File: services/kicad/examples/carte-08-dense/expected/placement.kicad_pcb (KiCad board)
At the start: 2 copper layers, 57.3 x 44 mm, 56 parts, among them J1 IN_5V, J10 IO0, J11 IO1, J12 IO2, J13 IO3, J14 IO4, J2 SWD, U1 STM32F103C8T6, U2 AMS1117-3.3

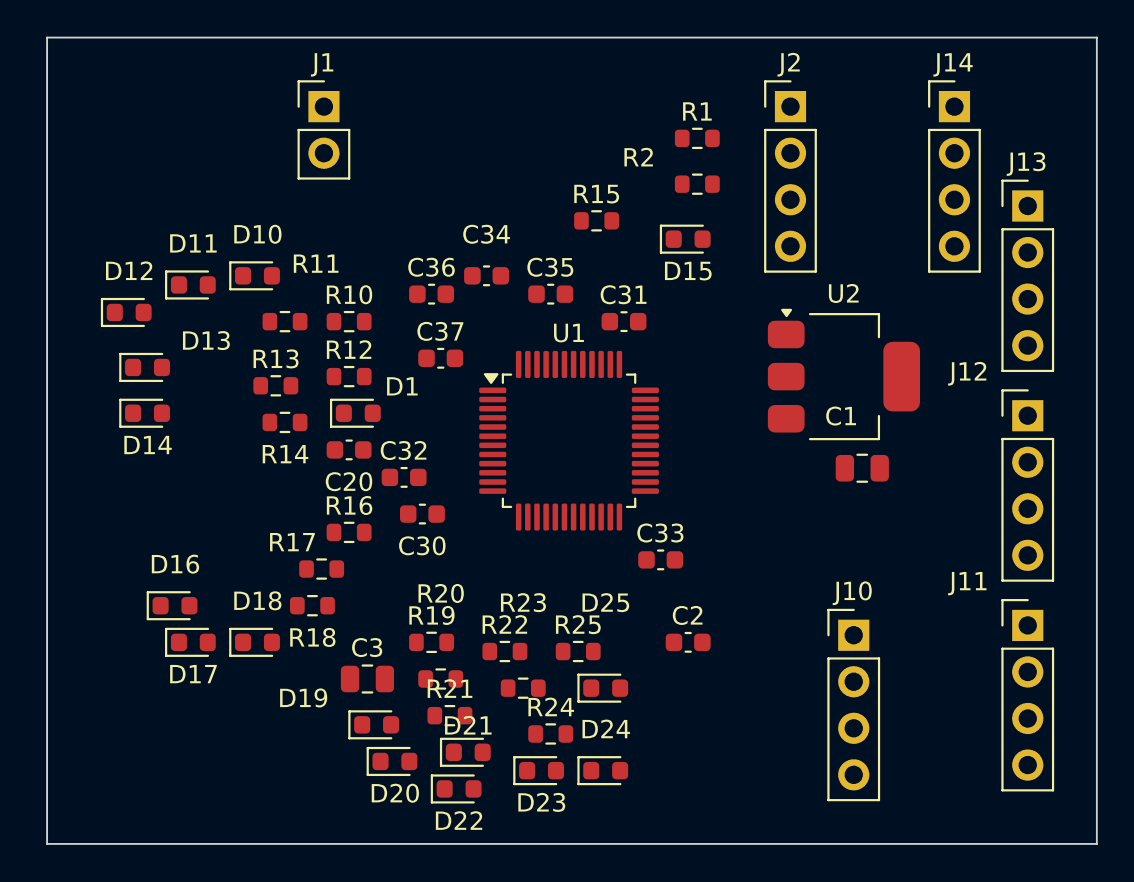
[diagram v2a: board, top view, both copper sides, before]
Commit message: fix(banc): le banc route comme la production — plafond 8, budget du client
D-2026-09-24-f. run_pipeline.py prenait 2 couches et 1800 s par défaut, et
carte-07 écrivait 2 en dur : dix cartes sur quinze ne pouvaient jamais
escalader, et la règle « toute connexion manquante fait monter » était
inerte dans le banc. Mesuré sur carte-07 : 97 %, seule la masse manquante,
« le palier suivant sera tenté »… puis retour à 2 couches.

Plafond par défaut 8 (client Pro Max), budget min(600 + 300 x plafond, 3600)
comme routingSearchBudgetS côté client. En production, rien ne change : le
plafond reste celui du plan.

Livraisons du jour, toutes vérifiées par kicad-cli et contre le schéma
(0 erreur bloquante, 0 connexion manquante, 0 court-circuit) :
carte-04, 05, 06, 08 (campagne de l'après-midi) et carte-09, 10 (4 couches).
Les boards versionnés de ces cartes court-circuitaient des nets du schéma.

Correction de ma propre erreur dans la doc : carte-07 n'avait jamais
escaladé ; les lignes « palier 4 et 6 » du journal étaient celles de
carte-08, démarrée la même minute.

Co-Authored-By: Claude Opus 5.5 <noreply@anthropic.com>
Claude-Session: https://claude.ai/code/session_01TnMqm4La2CxQHHB5K8aSSV
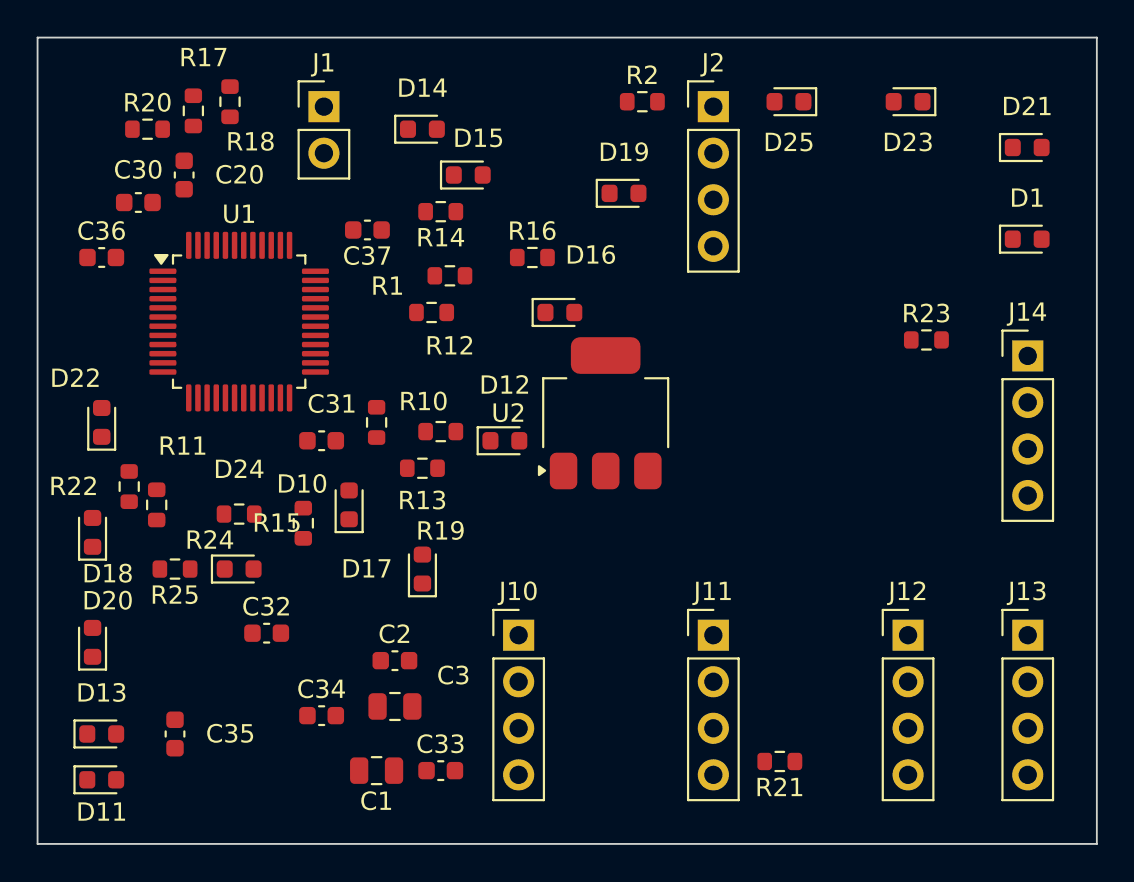
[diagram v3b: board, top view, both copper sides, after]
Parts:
- moved D21 44.9 mm to (140.0, 63.5)
- moved D23 41.6 mm to (133.5, 61.0), turned to 180 degrees
- moved D1 37.7 mm to (140.0, 68.5)
- moved R20 34.0 mm to (92.0, 62.5)
- moved D25 33.5 mm to (127.0, 61.0), turned to 180 degrees
- moved D19 32.0 mm to (118.0, 66.0)
- moved C35 31.6 mm to (93.5, 95.5), turned to 270 degrees
- moved C1 31.2 mm to (104.5, 97.5), turned to 180 degrees
- moved R23 29.1 mm to (134.5, 74.0)
- moved D22 27.9 mm to (89.5, 78.5), turned to 90 degrees
- moved R18 27.8 mm to (94.5, 61.5), turned to 270 degrees
- moved D11 27.5 mm to (89.5, 98.0)
- moved D16 26.4 mm to (114.5, 72.5)
- moved R17 26.0 mm to (96.5, 61.0), turned to 90 degrees
- moved C34 25.6 mm to (101.5, 94.5)
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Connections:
- C3 pad 1: Net-(C3-1) -> +3V3
- U1 pad 36: PWR_FLAG -> +3V3
- U1 pad 48: PWR_FLAG -> +3V3
- U1 pad 9: PWR_FLAG -> IO_L5
- U2 pad 2: Net-(U2-2) -> +3V3
- U2 pad 3: PWR_FLAG -> VIN
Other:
- board size 57.3 x 44 mm -> 57.8 x 44 mm
